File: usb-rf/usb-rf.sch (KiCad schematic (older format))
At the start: 38 parts, among them J1 USB_B_Micro, J2 SMA, J3 ARM 10 pin, U1 STM32L432KBUx, U2 XC6206PxxxMR, U3 USBLC6-2SC6, U4 nRF24L01P, Y1 16MHz

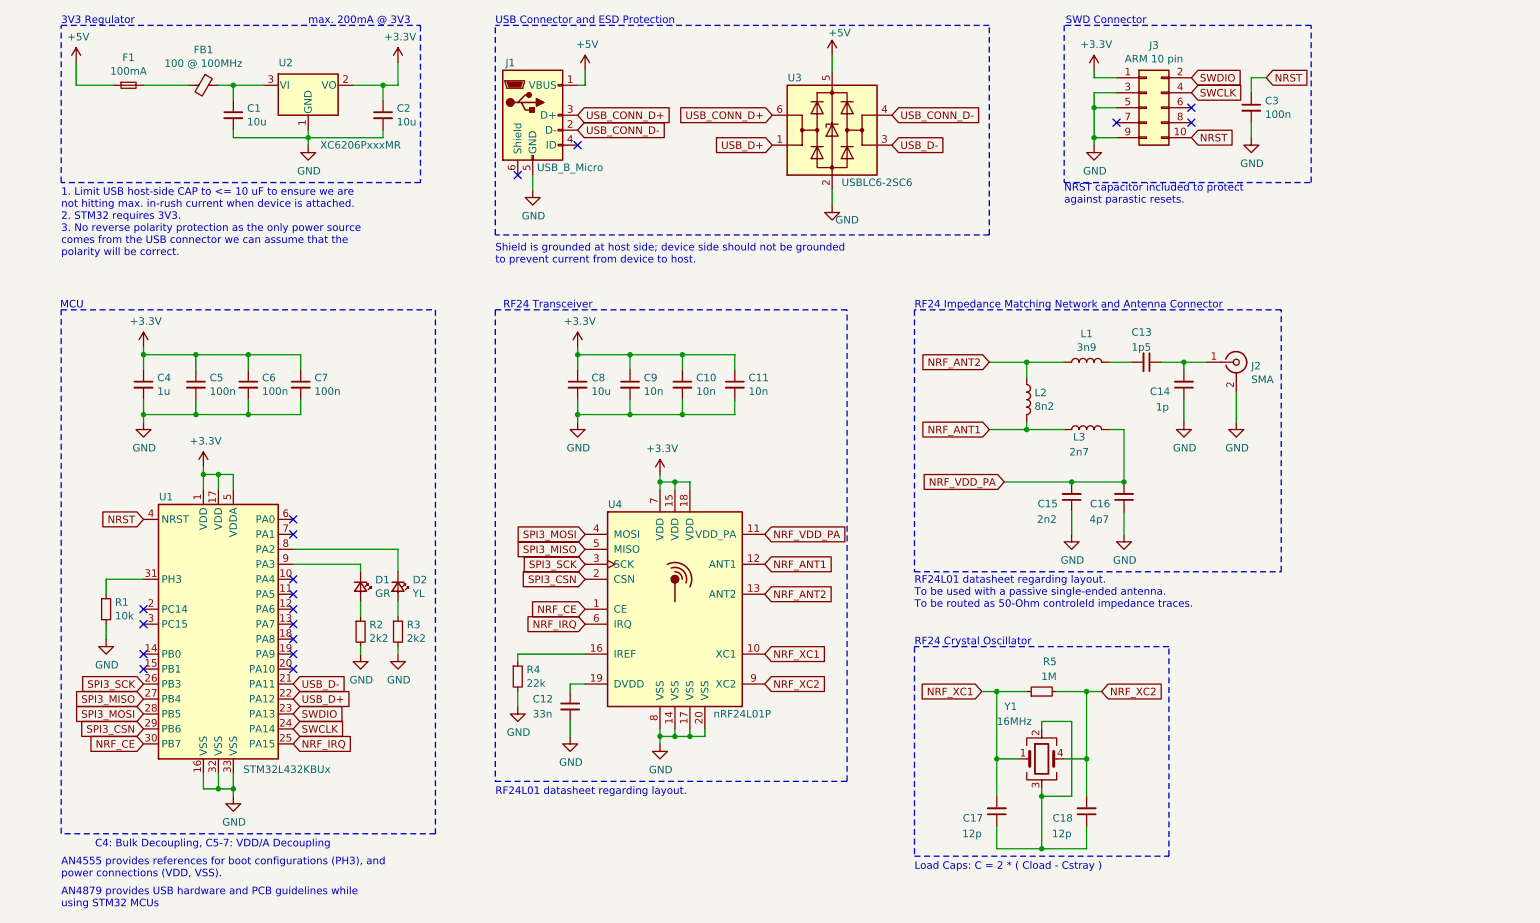
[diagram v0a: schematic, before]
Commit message: stm-rf: complete footprint lay out
add: power and ground planes

Signed-off-by: Sean Tedesco <stedesco@live.com>
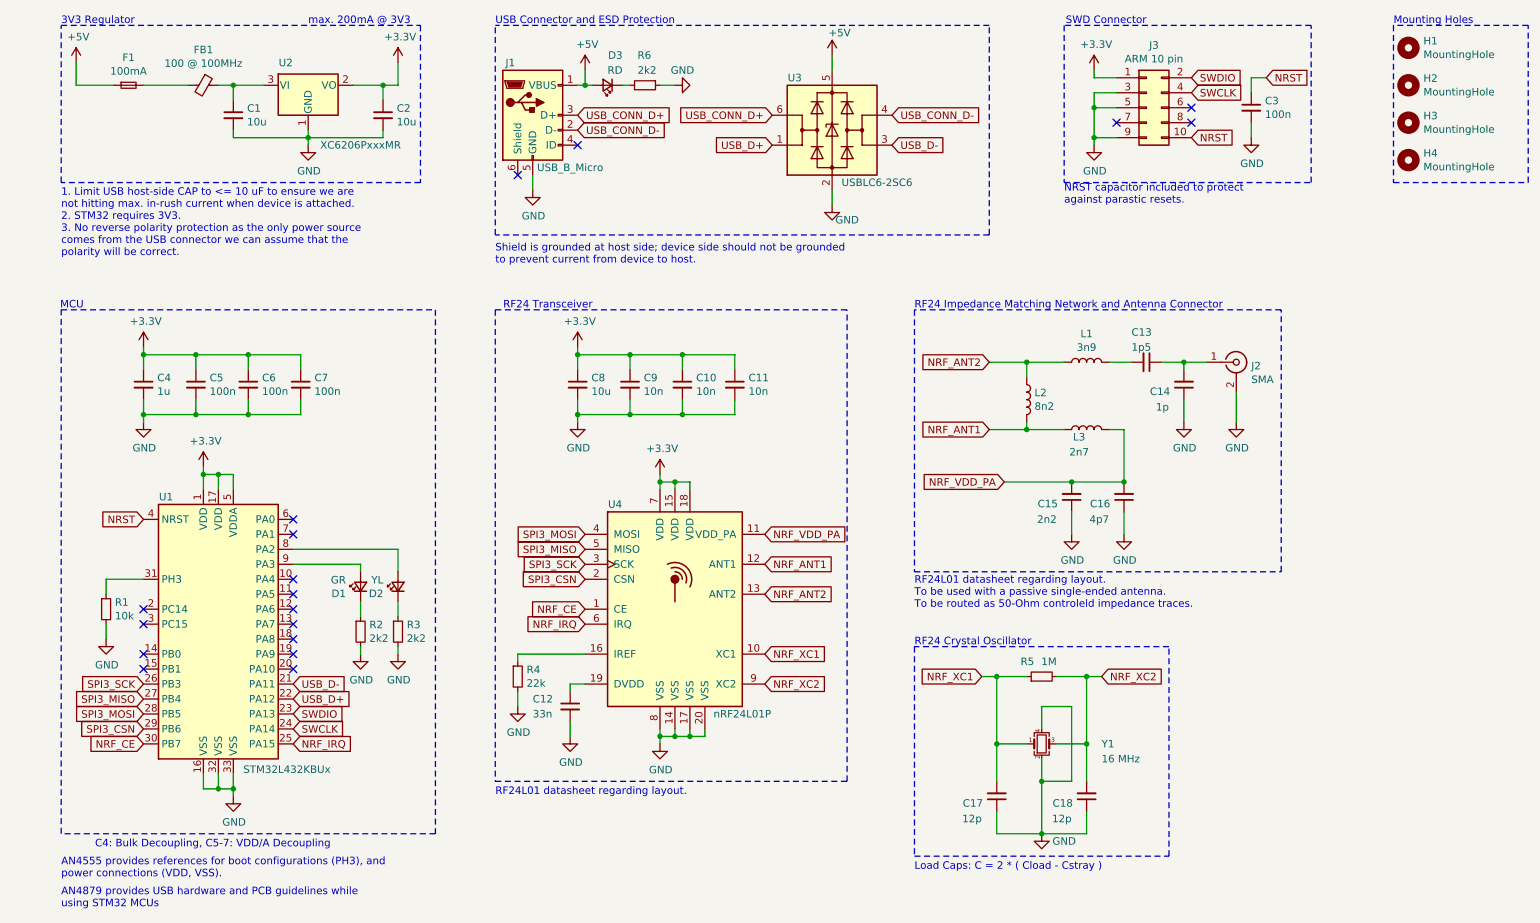
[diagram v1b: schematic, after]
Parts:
- removed Y1: 16MHz, Crystal:Crystal_SMD_3225-4Pin_3.2x2.5mm, symbol Device:Crystal_GND23
- added D3: RD, LED_SMD:LED_0603_1608Metric, symbol Device:LED_Small
- added H1, H2, H3, H4: MountingHole, MountingHole:MountingHole_2.2mm_M2_Pad, symbol Mechanical:MountingHole
- added R6: 2k2, Resistor_SMD:R_0603_1608Metric, symbol Device:R_Small
- added Y1: 16 MHz, Crystal:Crystal_SMD_3225-4Pin_3.2x2.5mm, symbol Device:Crystal_GND24_Small
- J3: footprint Connector_PinSocket_1.27mm:PinSocket_2x05_P1.27mm_Vertical_SMD -> Connector_PinHeader_1.27mm:PinHeader_2x05_P1.27mm_Vertical
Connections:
- net +5V: now also D3.2 (A)
- net GND: now also C17.1, C18.1, R6.1, Y1.2, Y1.4
- net NRF_XC1: now also Y1.1
- net NRF_XC2: now also Y1.3
- net at U1.8 (PA2): now also D2.2 (A); no longer D2.1 (K)
- net at U1.9 (PA3): now also D1.2 (A); no longer D1.1 (K)
- net at R3.1: now also D2.1 (K); no longer D2.2 (A)
- net at R2.1: now also D1.1 (K); no longer D1.2 (A)
- new net: D3.1 (K), R6.2
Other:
- note added: "Mounting Holes"
- moved on the sheet: C17, C18, D1, D2, R5
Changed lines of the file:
@@
 F 3 "~" V 2550 4350 50  0001 C CNN
 	1    2550 4350
-	0    1    1    0
+	0    -1   -1   0
 $EndComp
 $Comp
@@
 F 3 "~" V 2800 4350 50  0001 C CNN
 	1    2800 4350
-	0    1    1    0
+	0    -1   -1   0
 $EndComp
 $Comp
@@
 F 0 "J3" H 7850 1567 50  0000 C CNN
 F 1 "ARM 10 pin" H 7850 1476 50  0000 C CNN
-F 2 "Connector_PinSocket_1.27mm:PinSocket_2x05_P1.27mm_Vertical_SMD" H 7800 1150 50  0001 C CNN
+F 2 "Connector_PinHeader_1.27mm:PinHeader_2x05_P1.27mm_Vertical" H 7800 1150 50  0001 C CNN
 F 3 "~" H 7800 1150 50  0001 C CNN
 	1    7800 1150
@@
 L Device:R_Small R5
 U 1 1 61F12F19
-P 7100 5050
-F 0 "R5" V 7300 4950 50  0000 L CNN
-F 1 "1M" V 7200 4950 50  0000 L CNN
-F 2 "Resistor_SMD:R_0402_1005Metric" H 7100 5050 50  0001 C CNN
-F 3 "~" H 7100 5050 50  0001 C CNN
-	1    7100 5050
+P 7100 4950
+F 0 "R5" V 7200 5000 50  0000 L CNN
+F 1 "1M" V 7200 4850 50  0000 L CNN
+F 2 "Resistor_SMD:R_0402_1005Metric" H 7100 4950 50  0001 C CNN
+F 3 "~" H 7100 4950 50  0001 C CNN
+	1    7100 4950
 	0    -1   -1   0
-$EndComp
-$Comp
-L Device:Crystal_GND23 Y1
-U 1 1 61F16555
-P 7100 5500
-F 0 "Y1" H 6850 5850 50  0000 L CNN
-F 1 "16MHz" H 6800 5750 50  0000 L CNN
-F 2 "Crystal:Crystal_SMD_3225-4Pin_3.2x2.5mm" H 7100 5500 50  0001 C CNN
-F 3 "~" H 7100 5500 50  0001 C CNN
-	1    7100 5500
-	1    0    0    -1
 $EndComp
 $Comp
 L Device:C_Small C17
 U 1 1 61F16DDF
-P 6800 5850
-F 0 "C17" H 6892 5896 50  0000 L CNN
-F 1 "12p" H 6900 6000 50  0000 L CNN
-F 2 "Capacitor_SMD:C_0402_1005Metric" H 6800 5850 50  0001 C CNN
-F 3 "~" H 6800 5850 50  0001 C CNN
-	1    6800 5850
+P 6800 5750
+F 0 "C17" H 6892 5796 50  0000 L CNN
+F 1 "12p" H 6900 5900 50  0000 L CNN
+F 2 "Capacitor_SMD:C_0402_1005Metric" H 6800 5750 50  0001 C CNN
+F 3 "~" H 6800 5750 50  0001 C CNN
+	1    6800 5750
 	-1   0    0    1
 $EndComp
@@
 L Device:C_Small C18
 U 1 1 61F18048
-P 7400 5850
-F 0 "C18" H 7492 5896 50  0000 L CNN
-F 1 "12p" H 7500 6000 50  0000 L CNN
-F 2 "Capacitor_SMD:C_0402_1005Metric" H 7400 5850 50  0001 C CNN
-F 3 "~" H 7400 5850 50  0001 C CNN
-	1    7400 5850
+P 7400 5750
+F 0 "C18" H 7492 5796 50  0000 L CNN
+F 1 "12p" H 7500 5900 50  0000 L CNN
+F 2 "Capacitor_SMD:C_0402_1005Metric" H 7400 5750 50  0001 C CNN
+F 3 "~" H 7400 5750 50  0001 C CNN
+	1    7400 5750
 	-1   0    0    1
 $EndComp
 Wire Wire Line
-	7100 6100 7400 6100
-Wire Wire Line
-	7400 6100 7400 5950
-Wire Wire Line
-	6800 5950 6800 6100
-Wire Wire Line
-	6800 6100 7100 6100
-Connection ~ 7100 6100
-Wire Wire Line
-	6800 5750 6800 5500
-Wire Wire Line
-	6800 5500 6950 5500
-Wire Wire Line
-	6800 5500 6800 5050
-Wire Wire Line
-	6800 5050 7000 5050
-Connection ~ 6800 5500
-Wire Wire Line
-	7100 5750 7100 6100
-Wire Wire Line
-	7100 5700 7100 5750
-Connection ~ 7100 5750
-Wire Wire Line
-	7100 5300 7100 5250
-Wire Wire Line
-	7400 5750 7400 5500
-Wire Wire Line
-	7300 5250 7300 5750
-Wire Wire Line
-	7100 5750 7300 5750
-Wire Wire Line
-	7100 5250 7300 5250
-Wire Wire Line
-	7250 5500 7400 5500
-Wire Wire Line
-	7400 5500 7400 5050
-Wire Wire Line
-	7400 5050 7200 5050
-Connection ~ 7400 5500
-Text GLabel 6700 5050 0    50   Input ~ 0
+	7100 6000 7400 6000
+Wire Wire Line
+	7400 6000 7400 5850
+Wire Wire Line
+	6800 5850 6800 6000
+Wire Wire Line
+	6800 6000 7100 6000
+Connection ~ 7100 6000
+Wire Wire Line
+	6800 5650 6800 5400
+Wire Wire Line
+	6800 5400 6800 4950
+Wire Wire Line
+	6800 4950 7000 4950
+Connection ~ 6800 5400
+Wire Wire Line
+	7100 5650 7100 6000
+Connection ~ 7100 5650
+Wire Wire Line
+	7400 5650 7400 5400
+Wire Wire Line
+	7300 5150 7300 5650
+Wire Wire Line
+	7100 5650 7300 5650
+Wire Wire Line
+	7100 5150 7300 5150
+Wire Wire Line
+	7400 5400 7400 4950
+Wire Wire Line
+	7400 4950 7200 4950
+Connection ~ 7400 5400
+Text GLabel 6700 4950 0    50   Input ~ 0
 NRF_XC1
-Text GLabel 7500 5050 2    50   Input ~ 0
+Text GLabel 7500 4950 2    50   Input ~ 0
 NRF_XC2
 Wire Wire Line
-	6700 5050 6800 5050
-Connection ~ 6800 5050
-Wire Wire Line
-	7400 5050 7500 5050
-Connection ~ 7400 5050
+	6700 4950 6800 4950
+Connection ~ 6800 4950
+Wire Wire Line
+	7400 4950 7500 4950
+Connection ~ 7400 4950
 Wire Notes Line
 	6250 4750 6250 6150
@@
 Text Notes 6250 6250 0    50   ~ 0
 Load Caps: C = 2 * ( Cload - Cstray )
+$Comp
+L power:GND #PWR0128
+U 1 1 62102125
+P 7100 6000
+F 0 "#PWR0128" H 7100 5750 50  0001 C CNN
+F 1 "GND" H 7250 5950 50  0000 C CNN
+F 2 "" H 7100 6000 50  0001 C CNN
+F 3 "" H 7100 6000 50  0001 C CNN
+	1    7100 6000
+	1    0    0    -1
+$EndComp
+Wire Wire Line
+	7100 5150 7100 5300
+Wire Wire Line
+	7100 5500 7100 5650
+Wire Wire Line
+	7200 5400 7400 5400
+Wire Wire Line
+	6800 5400 7000 5400
+$Comp
+L Device:Crystal_GND24_Small Y1
+U 1 1 6211FB6F
+P 7100 5400
+F 0 "Y1" H 7500 5400 50  0000 L CNN
+F 1 "16 MHz" H 7500 5300 50  0000 L CNN
+F 2 "Crystal:Crystal_SMD_3225-4Pin_3.2x2.5mm" H 7100 5400 50  0001 C CNN
+F 3 "~" H 7100 5400 50  0001 C CNN
+	1    7100 5400
+	1    0    0    -1
+$EndComp
+$Comp
+L Mechanical:MountingHole H2
+U 1 1 61ED0476
+P 9550 1000
+F 0 "H2" H 9650 1046 50  0000 L CNN
+F 1 "MountingHole" H 9650 955 50  0000 L CNN
+F 2 "MountingHole:MountingHole_2.2mm_M2_Pad" H 9550 1000 50  0001 C CNN
+F 3 "~" H 9550 1000 50  0001 C CNN
+	1    9550 1000
+	1    0    0    -1
+$EndComp
+$Comp
+L Mechanical:MountingHole H3
+U 1 1 61ED0BB2
+P 9550 1250
+F 0 "H3" H 9650 1296 50  0000 L CNN
+F 1 "MountingHole" H 9650 1205 50  0000 L CNN
+F 2 "MountingHole:MountingHole_2.2mm_M2_Pad" H 9550 1250 50  0001 C CNN
+F 3 "~" H 9550 1250 50  0001 C CNN
+	1    9550 1250
+	1    0    0    -1
+$EndComp
+$Comp
+L Mechanical:MountingHole H4
+U 1 1 61ED1128
+P 9550 1500
+F 0 "H4" H 9650 1546 50  0000 L CNN
+F 1 "MountingHole" H 9650 1455 50  0000 L CNN
+F 2 "MountingHole:MountingHole_2.2mm_M2_Pad" H 9550 1500 50  0001 C CNN
+F 3 "~" H 9550 1500 50  0001 C CNN
+	1    9550 1500
+	1    0    0    -1
+$EndComp
+$Comp
+L Mechanical:MountingHole H1
+U 1 1 61ECFCEE
+P 9550 750
+F 0 "H1" H 9650 796 50  0000 L CNN
+F 1 "MountingHole" H 9650 705 50  0000 L CNN
+F 2 "MountingHole:MountingHole_2.2mm_M2_Pad" H 9550 750 50  0001 C CNN
+F 3 "~" H 9550 750 50  0001 C CNN
+	1    9550 750
+	1    0    0    -1
+$EndComp
+Wire Notes Line
+	9450 600  9450 1650
+Wire Notes Line
+	9450 1650 10350 1650
+Wire Notes Line
+	10350 1650 10350 600
+Wire Notes Line
+	10350 600  9450 600
+Text Notes 9450 600  0    50   ~ 0
+Mounting Holes
+$Comp
+L Device:LED_Small D3
+U 1 1 61EEF28E
+P 4200 1000
+F 0 "D3" H 4100 800 50  0000 L CNN
+F 1 "RD" H 4100 900 50  0000 L CNN
+F 2 "LED_SMD:LED_0603_1608Metric" V 4200 1000 50  0001 C CNN
+F 3 "~" V 4200 1000 50  0001 C CNN
+	1    4200 1000
+	-1   0    0    1
+$EndComp
+$Comp
+L Device:R_Small R6
+U 1 1 61EF03F4
+P 4450 1000
+F 0 "R6" V 4250 950 50  0000 L CNN
+F 1 "2k2" V 4350 950 50  0000 L CNN
+F 2 "Resistor_SMD:R_0603_1608Metric" H 4450 1000 50  0001 C CNN
+F 3 "~" H 4450 1000 50  0001 C CNN
+	1    4450 1000
+	0    1    1    0
+$EndComp
+$Comp
+L power:GND #PWR0129
+U 1 1 61F0E684
+P 4650 1000
+F 0 "#PWR0129" H 4650 750 50  0001 C CNN
+F 1 "GND" V 4750 950 50  0000 C CNN
+F 2 "" H 4650 1000 50  0001 C CNN
+F 3 "" H 4650 1000 50  0001 C CNN
+	1    4650 1000
+	0    -1   -1   0
+$EndComp
+Wire Wire Line
+	4050 1000 4100 1000
+Connection ~ 4050 1000
+Wire Wire Line
+	4300 1000 4350 1000
+Wire Wire Line
+	4550 1000 4650 1000
 $EndSCHEMATC

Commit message: usb-rf: include step and rf guard ring
just need manufacturing files!

Signed-off-by: Sean Tedesco <stedesco@live.com>
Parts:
- J1: footprint Connector_USB:USB_Micro-B_Molex-105017-0001 -> footprints:USB_Micro-B_Molex-105017-0001-SeanCopy
- J2: footprint Connector_Coaxial:SMA_Samtec_SMA-J-P-X-ST-EM1_EdgeMount -> footprints:SMA_Samtec_SMA-J-P-X-ST-EM1_EdgeMount-SeanCopyy
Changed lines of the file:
@@
 F 0 "J1" H 3550 1550 50  0000 C CNN
 F 1 "USB_B_Micro" H 3950 850 50  0000 C CNN
-F 2 "Connector_USB:USB_Micro-B_Molex-105017-0001" H 3850 1150 50  0001 C CNN
+F 2 "footprints:USB_Micro-B_Molex-105017-0001-SeanCopy" H 3850 1150 50  0001 C CNN
 F 3 "~" H 3850 1150 50  0001 C CNN
 	1    3700 1200
@@
 F 0 "J2" H 8500 2825 50  0000 L CNN
 F 1 "SMA" H 8500 2734 50  0000 L CNN
-F 2 "Connector_Coaxial:SMA_Samtec_SMA-J-P-X-ST-EM1_EdgeMount" H 8400 2850 50  0001 C CNN
+F 2 "footprints:SMA_Samtec_SMA-J-P-X-ST-EM1_EdgeMount-SeanCopyy" H 8400 2850 50  0001 C CNN
 F 3 " ~" H 8400 2850 50  0001 C CNN
 	1    8400 2850

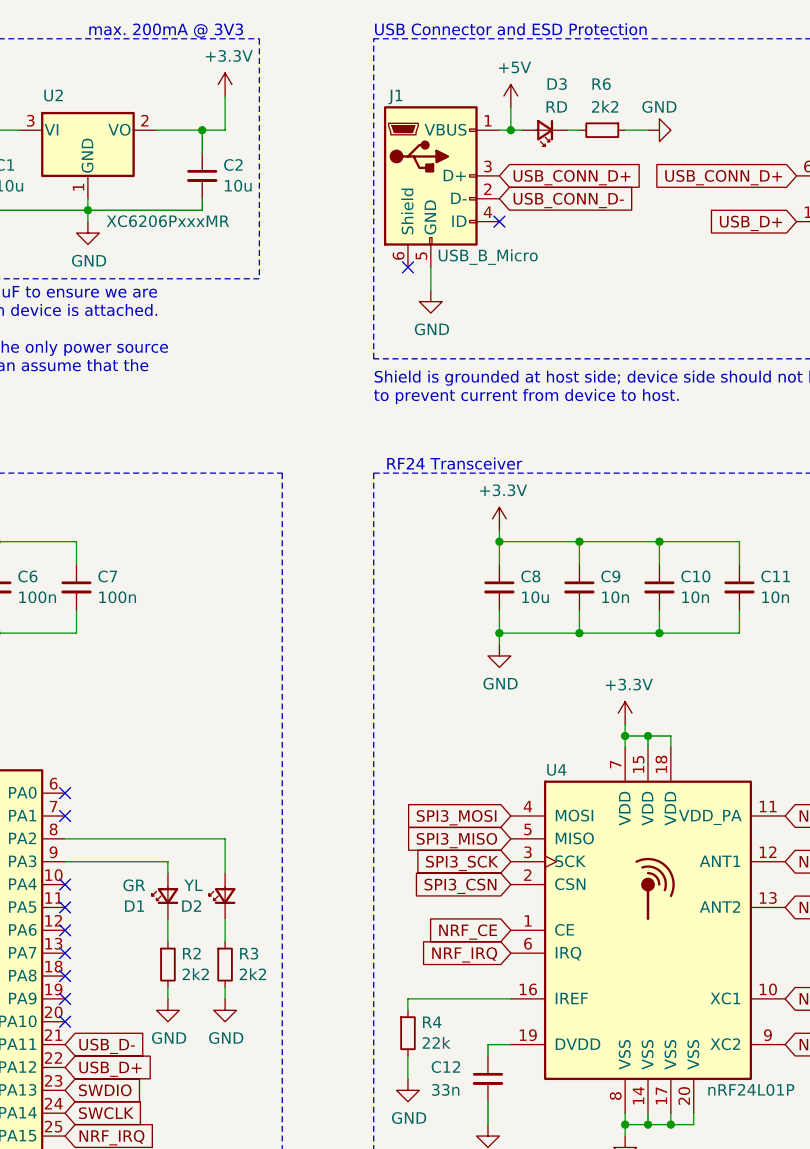
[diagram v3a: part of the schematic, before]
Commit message: usb-rf: include files for fab house
Signed-off-by: Sean Tedesco <stedesco@live.com>
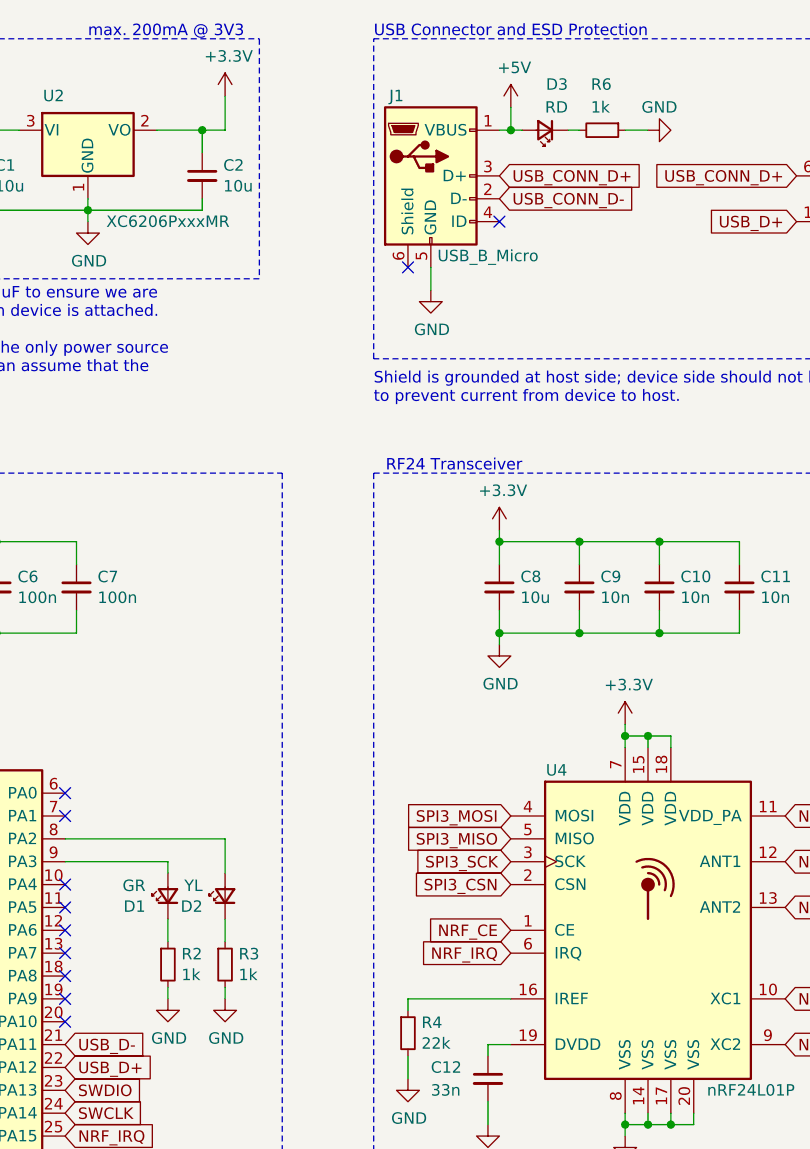
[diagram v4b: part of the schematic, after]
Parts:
- R2, R3, R6: value 2k2 -> 1k
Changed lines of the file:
@@
 P 2800 4650
 F 0 "R3" H 2859 4696 50  0000 L CNN
-F 1 "2k2" H 2859 4605 50  0000 L CNN
+F 1 "1k" H 2859 4605 50  0000 L CNN
 F 2 "Resistor_SMD:R_0603_1608Metric" H 2800 4650 50  0001 C CNN
 F 3 "~" H 2800 4650 50  0001 C CNN
@@
 P 2550 4650
 F 0 "R2" H 2609 4696 50  0000 L CNN
-F 1 "2k2" H 2609 4605 50  0000 L CNN
+F 1 "1k" H 2609 4605 50  0000 L CNN
 F 2 "Resistor_SMD:R_0603_1608Metric" H 2550 4650 50  0001 C CNN
 F 3 "~" H 2550 4650 50  0001 C CNN
@@
 P 4450 1000
 F 0 "R6" V 4250 950 50  0000 L CNN
-F 1 "2k2" V 4350 950 50  0000 L CNN
+F 1 "1k" V 4350 950 50  0000 L CNN
 F 2 "Resistor_SMD:R_0603_1608Metric" H 4450 1000 50  0001 C CNN
 F 3 "~" H 4450 1000 50  0001 C CNN
